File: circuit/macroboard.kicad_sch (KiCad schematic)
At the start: 10 parts, among them SW13 SW_Push, SW15 SW_SPDT, SW16 SW_SPDT, U1 ATmega32U4-A

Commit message: add reset switch
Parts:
- added RESET: SW_Push, Button_Switch_THT:SW_PUSH_6mm, symbol Switch:SW_Push
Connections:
- net GND: now also RESET.1
- net at U1.13 (~{RESET}): now also RESET.2
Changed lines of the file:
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@@
+	(wire
+		(pts
+			(xy 186.69 39.37) (xy 186.69 41.91)
+		)
+		(stroke
+			(width 0)
+			(type default)
+		)
+	)
 	(wire
 		(pts
@@
 		(pts
 			(xy 231.14 49.53) (xy 233.68 49.53)
+		)
+		(stroke
+			(width 0)
+			(type default)
+		)
+	)
+	(wire
+		(pts
+			(xy 190.5 39.37) (xy 186.69 39.37)
 		)
 		(stroke
@@
 	)
 	(symbol
+		(lib_id "power:GND")
+		(at 186.69 41.91 0)
+		(unit 1)
+		(exclude_from_sim no)
+		(in_bom yes)
+		(on_board yes)
+		(dnp no)
+		(fields_autoplaced yes)
+		(property "Reference" "#PWR030"
+			(at 186.69 48.26 0)
+			(effects
+				(font
+					(size 1.27 1.27)
+				)
+				(hide yes)
+			)
+		)
+		(property "Value" "GND"
+			(at 186.69 46.99 0)
+			(effects
+				(font
+					(size 1.27 1.27)
+				)
+			)
+		)
+		(property "Footprint" ""
+			(at 186.69 41.91 0)
+			(effects
+				(font
+					(size 1.27 1.27)
+				)
+				(hide yes)
+			)
+		)
+		(property "Datasheet" ""
+			(at 186.69 41.91 0)
+			(effects
+				(font
+					(size 1.27 1.27)
+				)
+				(hide yes)
+			)
+		)
+		(property "Description" "Power symbol creates a global label with name \"GND\" , ground"
+			(at 186.69 41.91 0)
+			(effects
+				(font
+					(size 1.27 1.27)
+				)
+				(hide yes)
+			)
+		)
+		(pin "1"
+		)
+		(instances
+			(project "macroboard"
+				(path "/eb2ff33f-8c2d-40be-bc06-8483c3a89847"
+					(reference "#PWR030")
+					(unit 1)
+				)
+			)
+		)
+	)
+	(symbol
 		(lib_id "Mechanical:MountingHole")
 		(at 135.89 30.48 0)
@@
 					(unit 1)
 				)
+			)
+		)
+	)
+	(symbol
+		(lib_id "Switch:SW_Push")
+		(at 195.58 39.37 0)
+		(unit 1)
+		(exclude_from_sim no)
+		(in_bom yes)
+		(on_board yes)
+		(dnp no)
+		(fields_autoplaced yes)
+		(property "Reference" "RESET"
+			(at 195.58 31.75 0)
+			(effects
+				(font
+					(size 1.27 1.27)
+				)
+			)
+		)
+		(property "Value" "SW_Push"
+			(at 195.58 34.29 0)
+			(effects
+				(font
+					(size 1.27 1.27)
+				)
+			)
+		)
+		(property "Footprint" "Button_Switch_THT:SW_PUSH_6mm"
+			(at 195.58 34.29 0)
+			(effects
+				(font
+					(size 1.27 1.27)
+				)
+				(hide yes)
+			)
+		)
+		(property "Datasheet" "~"
+			(at 195.58 34.29 0)
+			(effects
+				(font
+					(size 1.27 1.27)
+				)
+				(hide yes)
+			)
+		)
+		(property "Description" "Push button switch, generic, two pins"
+			(at 195.58 39.37 0)
+			(effects
+				(font
+					(size 1.27 1.27)
+				)
+				(hide yes)
+			)
+		)
+		(pin "1"
+		)
+		(pin "2"
+		)
+		(instances
+			(project "macroboard"
+				(path "/eb2ff33f-8c2d-40be-bc06-8483c3a89847"
+					(reference "RESET")
+					(unit 1)
+				)

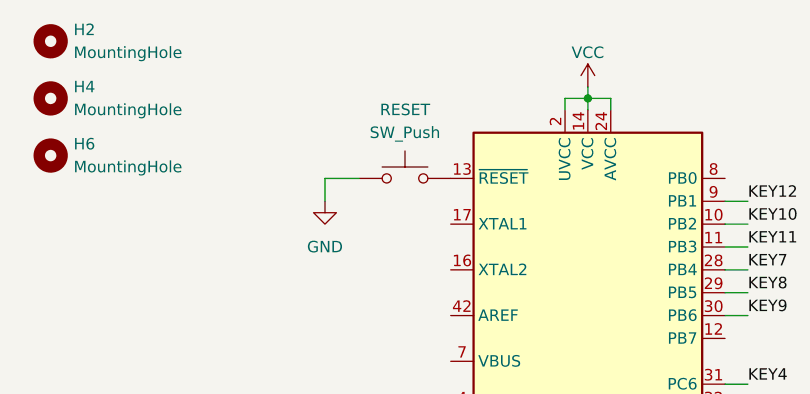
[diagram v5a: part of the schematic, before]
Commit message: fix wrong pin distance on Arduino micro footprint
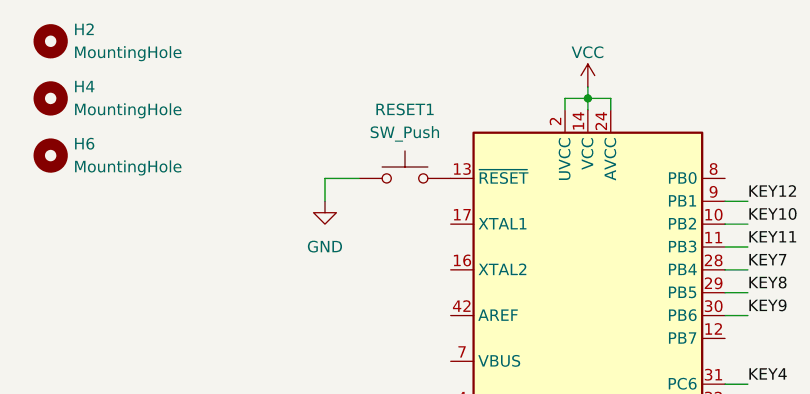
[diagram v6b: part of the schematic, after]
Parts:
- renumbered RESET to RESET1
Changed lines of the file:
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@@
 		(dnp no)
 		(fields_autoplaced yes)
-		(property "Reference" "RESET"
+		(property "Reference" "RESET1"
 			(at 195.58 31.75 0)
 			(effects
@@
 			(project "macroboard"
 				(path "/eb2ff33f-8c2d-40be-bc06-8483c3a89847"
-					(reference "RESET")
+					(reference "RESET1")
 					(unit 1)
 				)
